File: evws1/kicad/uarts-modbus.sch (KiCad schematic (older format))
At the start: 41 parts, among them J11 USB 2.0 Mini, J12 USB 2.0 Mini, T1 header, T3 header, U10 max485esa, U5 ch340g, U6 ch340g, Y2 12MHz, Y3 12MHz

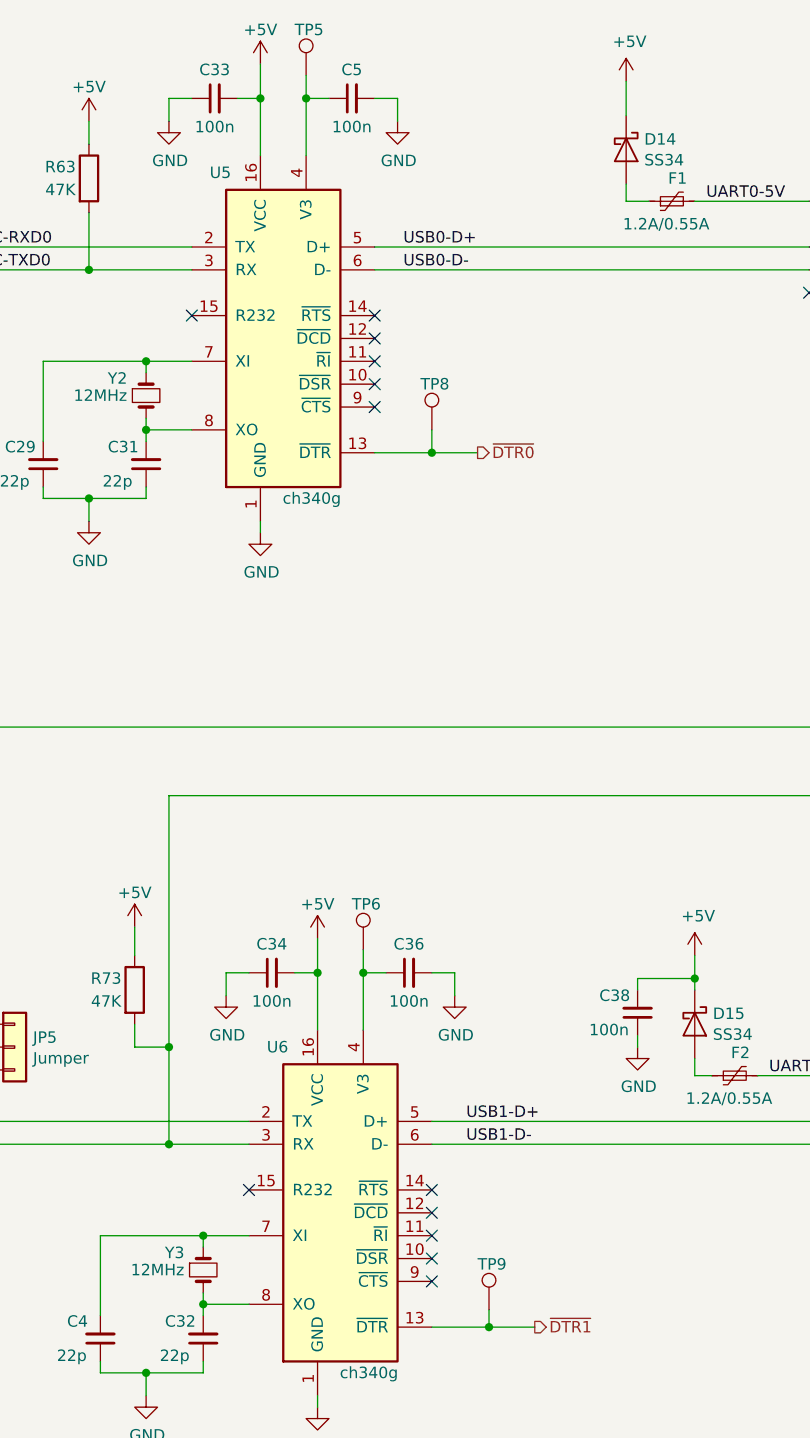
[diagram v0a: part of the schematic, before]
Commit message: fixing project problems, cause by renaming directory
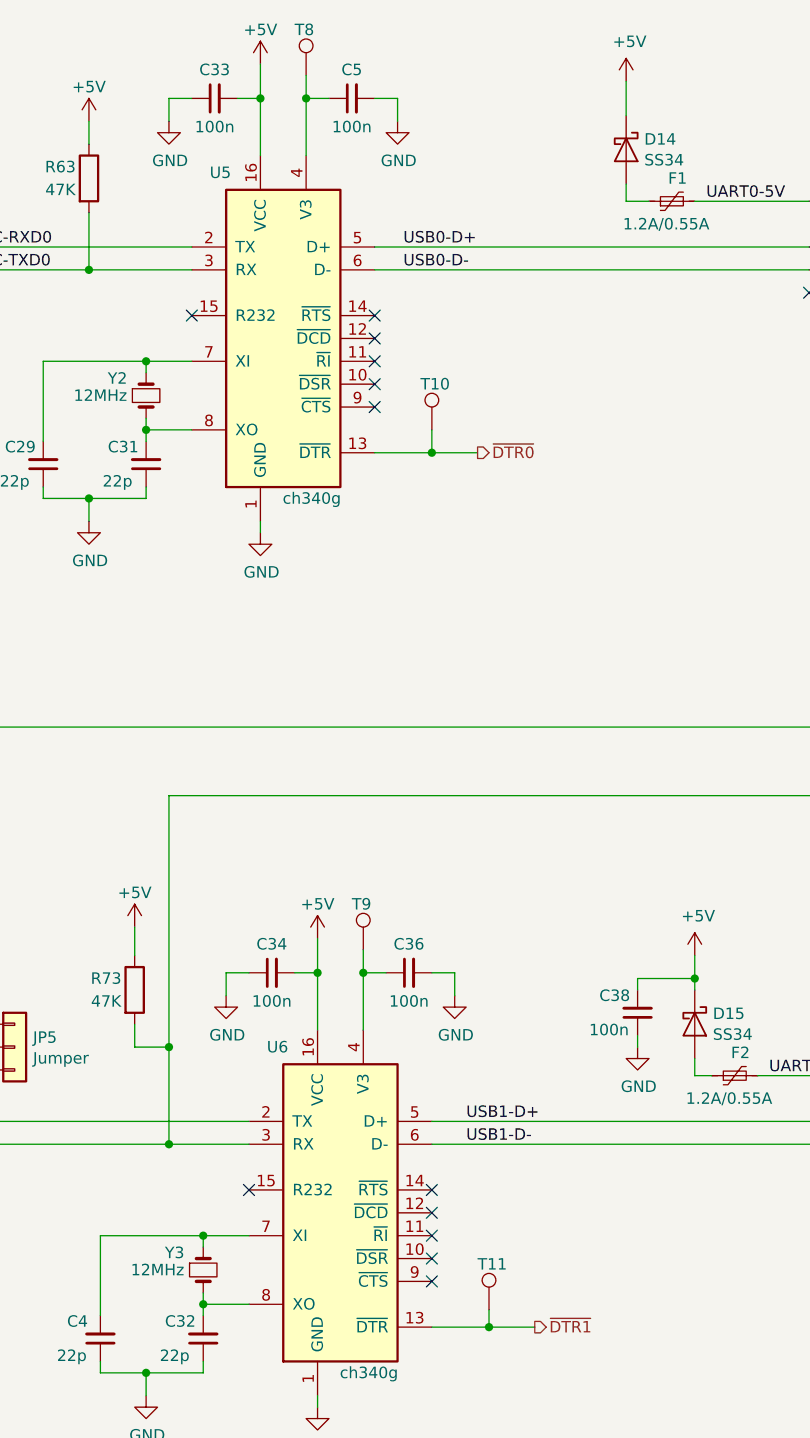
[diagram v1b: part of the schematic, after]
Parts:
- renumbered TP8 to T10, TP9 to T11, TP5 to T8, TP6 to T9
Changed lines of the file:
@@
 P 3100 1150
 AR Path="/5E0A3961/5E2A603E" Ref="TP?"  Part="1"
-AR Path="/5E0A3961/5E20BE9A/5E2A603E" Ref="TP5"  Part="1"
-F 0 "TP5" H 3050 1350 50  0000 L CNN
+AR Path="/5E0A3961/5E20BE9A/5E2A603E" Ref="T8"  Part="1"
+F 0 "T8" H 3050 1350 50  0000 L CNN
 F 1 "TestPoint" H 3158 1179 50  0001 L CNN
 F 2 "Wire_Pads:SolderWirePad_single_0-8mmDrill" H 3300 1150 50  0001 C CNN
@@
 P 3350 4975
 AR Path="/5E0A3961/5E2AEE03" Ref="TP?"  Part="1"
-AR Path="/5E0A3961/5E20BE9A/5E2AEE03" Ref="TP6"  Part="1"
-F 0 "TP6" H 3300 5175 50  0000 L CNN
+AR Path="/5E0A3961/5E20BE9A/5E2AEE03" Ref="T9"  Part="1"
+F 0 "T9" H 3300 5175 50  0000 L CNN
 F 1 "TestPoint" H 3408 5004 50  0001 L CNN
 F 2 "Wire_Pads:SolderWirePad_single_0-8mmDrill" H 3550 4975 50  0001 C CNN
@@
 P 3650 2700
 AR Path="/5E0A3961/601D002C" Ref="TP?"  Part="1"
-AR Path="/5E0A3961/5E20BE9A/601D002C" Ref="TP8"  Part="1"
-F 0 "TP8" H 3600 2900 50  0000 L CNN
+AR Path="/5E0A3961/5E20BE9A/601D002C" Ref="T10"  Part="1"
+F 0 "T10" H 3600 2900 50  0000 L CNN
 F 1 "TestPoint" H 3708 2729 50  0001 L CNN
 F 2 "Wire_Pads:SolderWirePad_single_0-8mmDrill" H 3850 2700 50  0001 C CNN
@@
 P 3900 6550
 AR Path="/5E0A3961/601D0033" Ref="TP?"  Part="1"
-AR Path="/5E0A3961/5E20BE9A/601D0033" Ref="TP9"  Part="1"
-F 0 "TP9" H 3850 6750 50  0000 L CNN
+AR Path="/5E0A3961/5E20BE9A/601D0033" Ref="T11"  Part="1"
+F 0 "T11" H 3850 6750 50  0000 L CNN
 F 1 "TestPoint" H 3958 6579 50  0001 L CNN
 F 2 "Wire_Pads:SolderWirePad_single_0-8mmDrill" H 4100 6550 50  0001 C CNN
